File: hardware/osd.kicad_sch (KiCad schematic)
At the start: 17 parts, among them U18 SN74LVC1G3157DTBR, U19 TLV9061IDPWR, U20 TLV3201AIDBVR

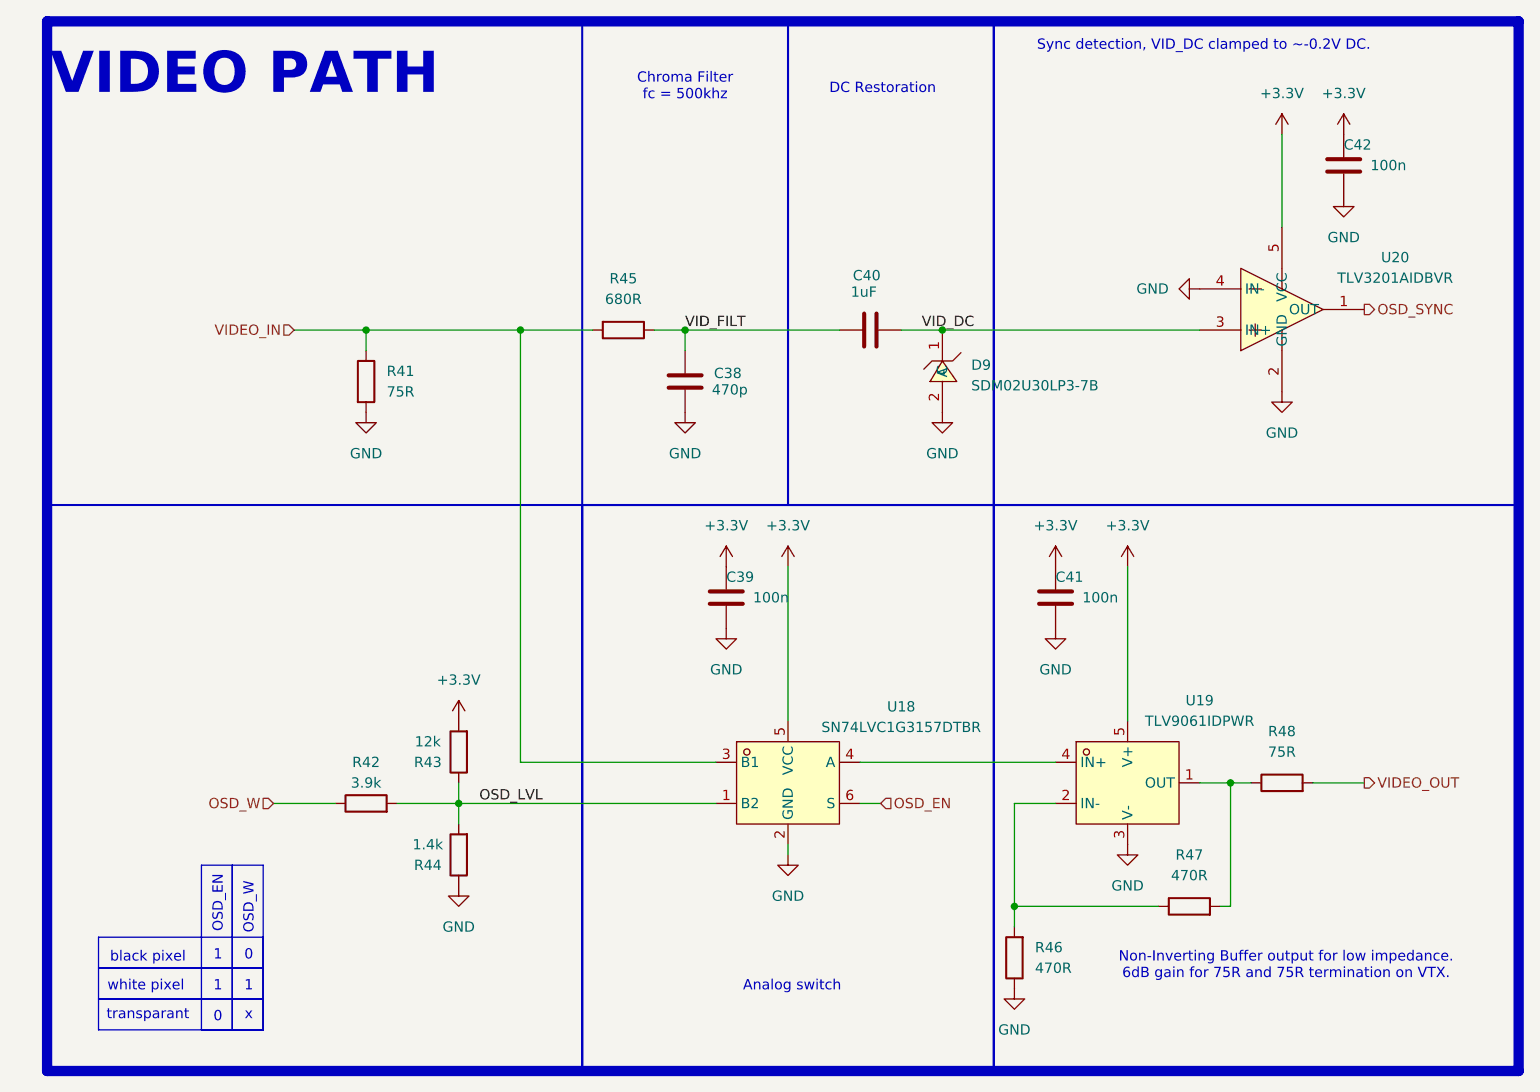
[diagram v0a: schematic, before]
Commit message: Rev 2 (RP2354A): finalize design, update docs, clean repo (#5)
* docs(readme): add analog OSD BOM to Rev 2 change list

Document OSD debugging findings and component changes as a new
Analog OSD section in the Rev 2 Change List:
- HW-12: U19 op-amp TLV9061IDPWR -> COS8051SOT (175MHz video-grade RRIO)
- HW-13: output front-end add AC-couple + DC-restore, power U19 from +5V
- HW-14: U20 comparator TLV3201AIDBVR -> TLV7031DPWR (push-pull, X2SON, ~75% smaller)
- HW-15: add OSD_EN select pull-down (datasheet-required, defaults to pass-through)
- U18 / D9 verified correct, no change; OSD GPIO mapping noted (PA4/5/6)

Also fix HW-11 beeper GPIO: GPIO6 -> GPIO7 (GPIO6 is OSD_SYNC per netlist).

Co-Authored-By: Claude Opus 4.8 (1M context) <noreply@anthropic.com>

* many tiny improvements

- I/O correctness
- SPI0/SPI1/I2C0 bus corrections
- decoupling of DVDD
- ADC_AVDD as per RPi documents
- removal of SBUS
- connect ESC serial
- remove RUN RC-circuit as per RPi documentation
- some more cleanup for readability
- gyro CLKIN decision
- I2C 4.7k pullup

* RP2354A

* piu1

* switch spi

* Update OpenFC.kicad_pcb

* routex2

* some minor tweaks

- remove some unnecessary resistors
- slightly higher 10V rail to account for voltage drop
- some cleanup
- simpler PG 1.8V circuit

* Update imu.kicad_sch

* LED resistors

Also reduced the amount of different resistors for cheaper assembly

* Delete leds.kicad_sch

* remove some unneeded decoupling caps from RP2350

* update MOSFET part numbers

* OSD

* ROUTE

* clean libs

* details

* led names

* Clean routing

* docs: rewrite README + CLAUDE.md for finalized Rev 2 (RP2354A)

Rev 2 is a substantial redesign that the docs no longer matched. Updated
both to the actual schematic, verified from the current netlist:

- MCU: RP2354B (QFN-80, GPIO0-47) -> RP2354A (QFN-60, GPIO0-29). Full GPIO
  map re-derived from the netlist + QFN-60 pinout; all 30 GPIO documented.
- IMU moved to SPI1, microSD to SPI0; ref designators re-annotated
  (op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
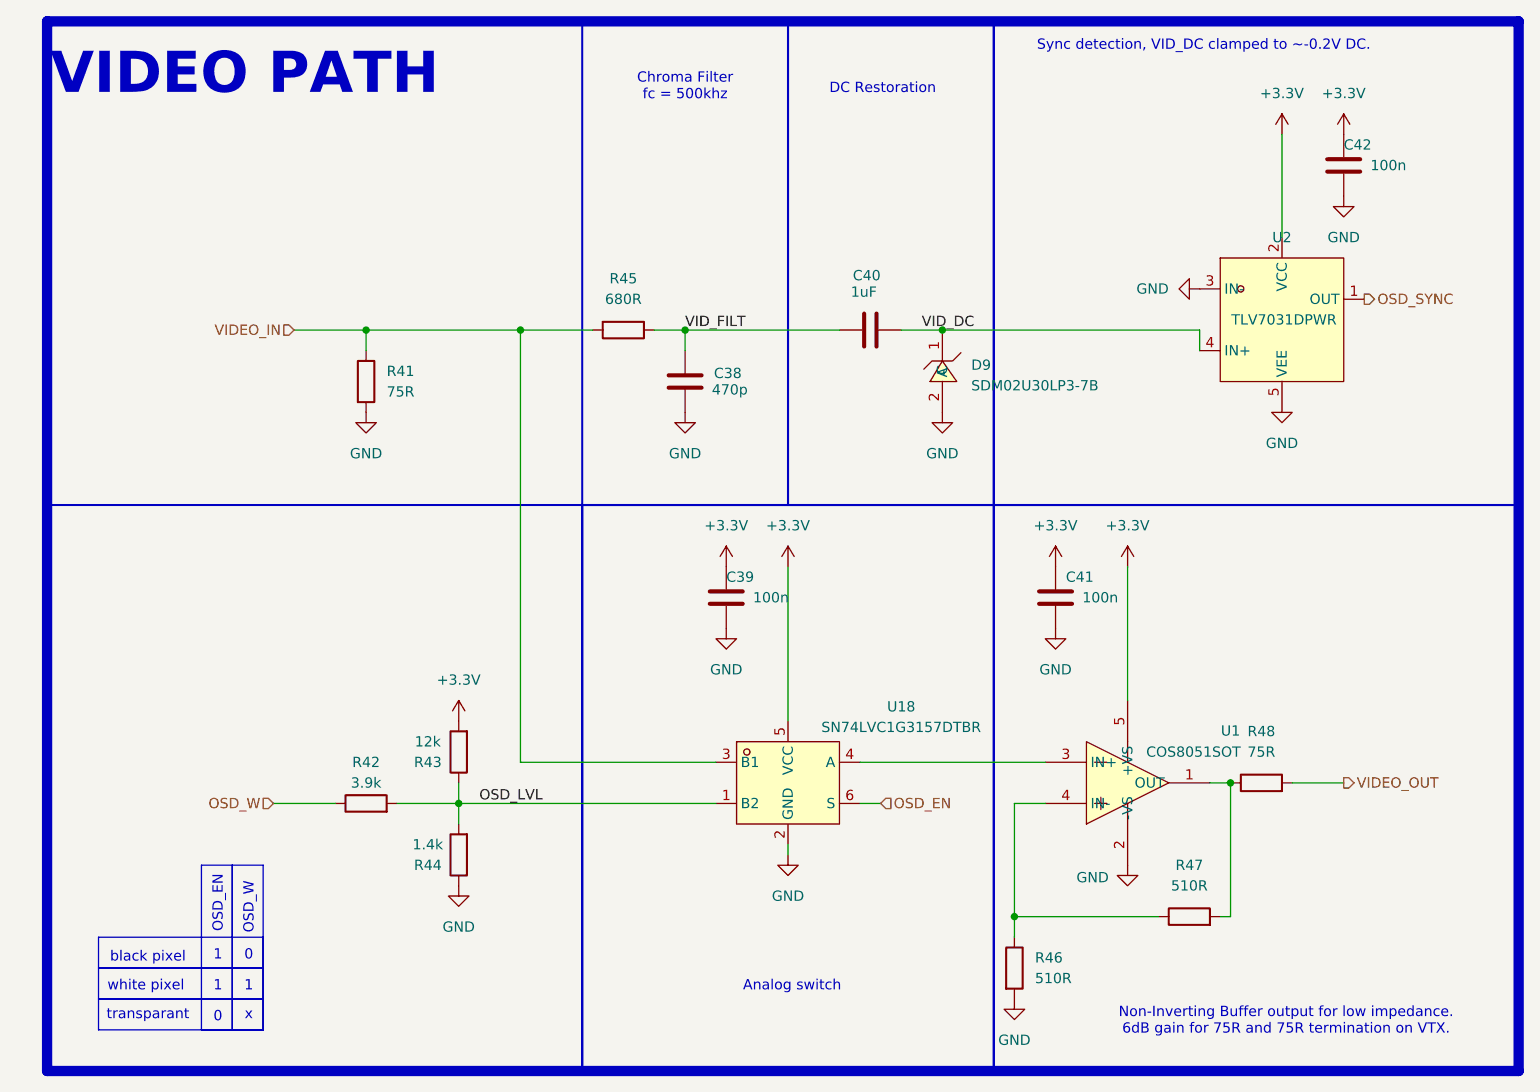
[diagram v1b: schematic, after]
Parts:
- removed U19: TLV9061IDPWR, lib:X2SON-4_L0.8-W0.8-P0.48-TL-DPW, symbol lib:TLV9061IDPWR
- removed U20: TLV3201AIDBVR, lib:SOT-23-5_L3.0-W1.7-P0.95-LS2.8-BR, symbol lib:TLV3201AIDBVR
- added U1: COS8051SOT, lib:SOT-23-5_L3.0-W1.7-P0.95-LS2.8-BR, symbol lib:COS8051SOT
- added U2: TLV7031DPWR, lib:X2SON-4_L0.8-W0.8-P0.48-TL-A, symbol lib:TLV7031DPWR
- R46, R47: value 470R -> 510R; LCSC C473464 -> C57784; MPN 0201WMF4700TEE -> (none); Manufacturer UNI-ROYAL -> (none)
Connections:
- net +3.3V: now also U1.5 (+VS), U2.2 (VCC)
- net GND: now also R46.2, U1.2 (-VS), U2.3 (IN-), U2.5 (VEE); no longer R46.1
- net OSD_SYNC: now also U2.1 (OUT)
- net VID_DC: now also U2.4 (IN+)
- net at R47.2, R48.1: now also U1.1 (OUT)
- net at R47.1: now also R46.1, U1.4 (IN-); no longer R46.2
- net at U18.4 (A): now also U1.3 (IN+)
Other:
- moved on the sheet: R48
